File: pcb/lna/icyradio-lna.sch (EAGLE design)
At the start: 15 parts, among them U1 ADL5601

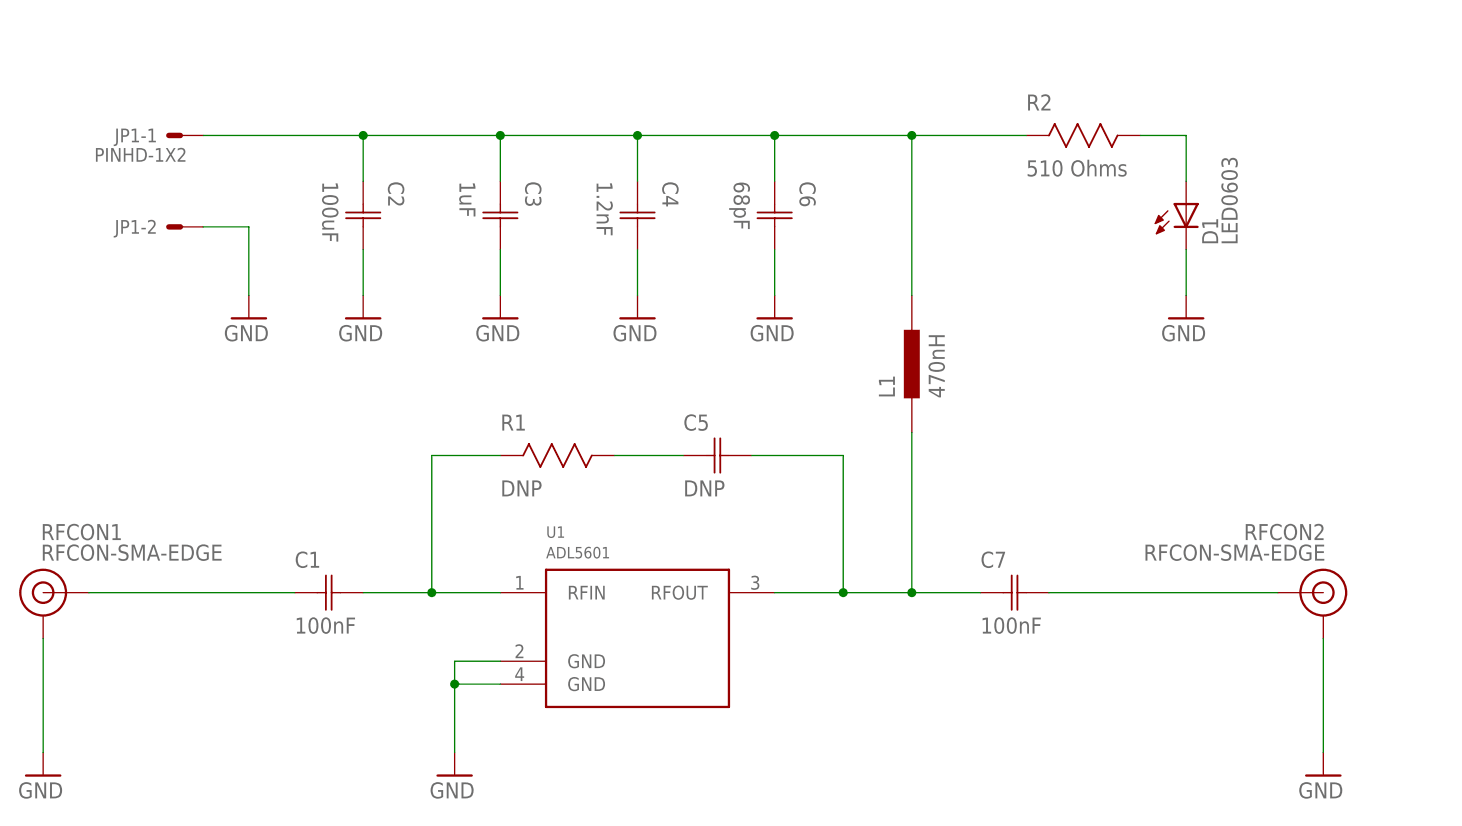
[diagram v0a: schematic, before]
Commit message: Sync library updates on LNA PCB
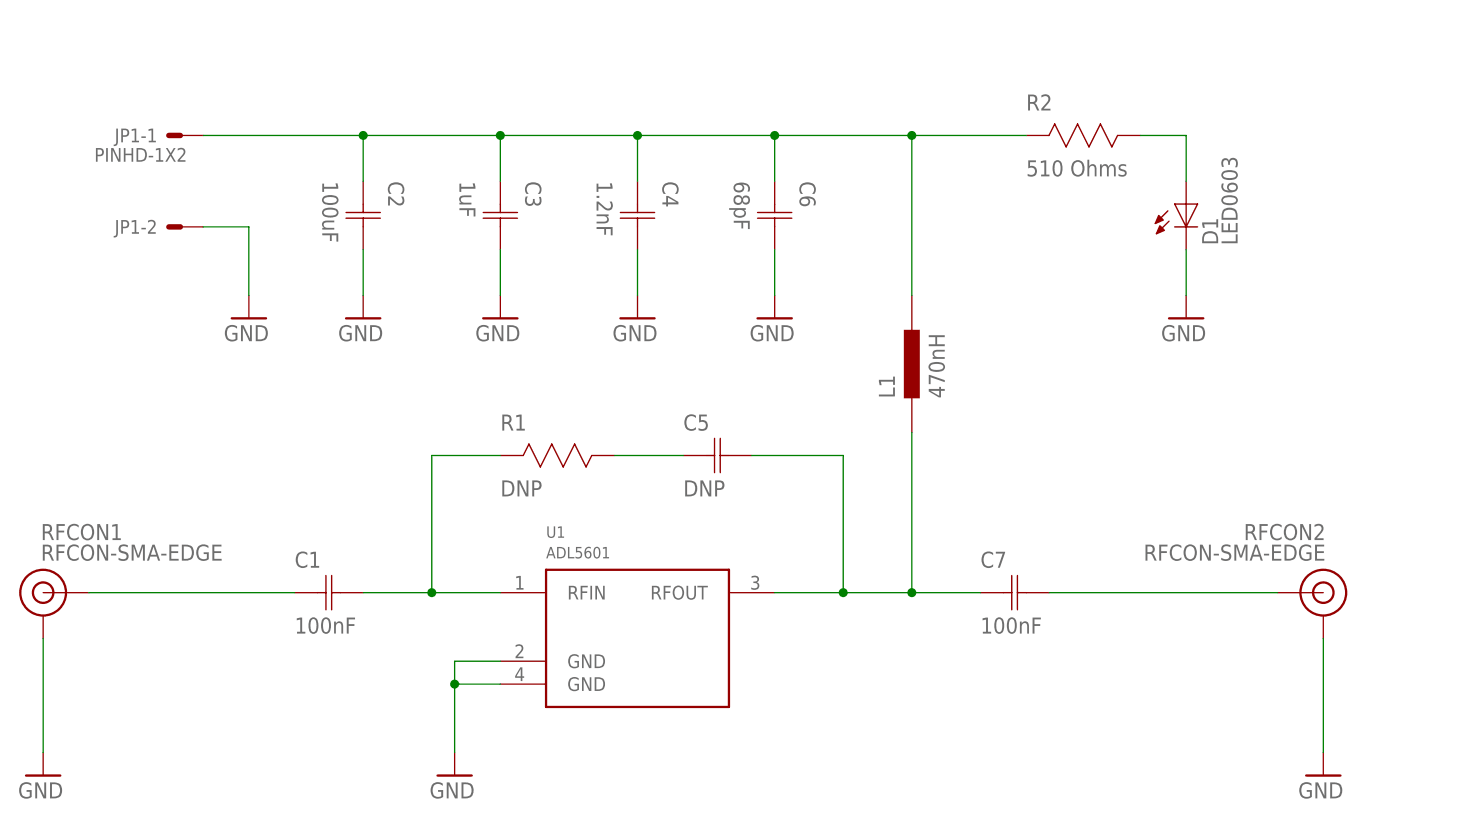
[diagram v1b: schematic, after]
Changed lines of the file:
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@@
 </classes>
 <parts>
-<part name="FRAME1" library="Frame" deviceset="A4-LANDSCAPE" device="">
-<attribute name="CNAME" value=""/>
-<attribute name="CREVISION" value=""/>
-<attribute name="DESIGNER" value=""/>
-</part>
 <part name="RFCON2" library="RF Connector" deviceset="RFCON" device="-SMA-EDGE"/>
 <part name="GND9" library="Supply Symbol" deviceset="GND" device=""/>
@@
 <part name="C2" library="Capacitor" deviceset="CAPACITOR" device="-1206" value="100uF"/>
 <part name="GND3" library="Supply Symbol" deviceset="GND" device=""/>
+<part name="FRAME1" library="Frame" deviceset="A4-LANDSCAPE" device=""/>
 </parts>
 <sheets>
@@
 </plain>
 <instances>
-<instance part="FRAME1" gate="G$1" x="0" y="0" smashed="yes">
-<attribute name="DRAWING_NAME" x="165.1" y="15.494" size="2.54" layer="94" font="vector"/>
-<attribute name="LAST_DATE_TIME" x="165.1" y="10.414" size="2.286" layer="94" font="vector"/>
-<attribute name="SHEET" x="179.07" y="5.334" size="2.54" layer="94" font="vector"/>
-<attribute name="DESIGNER" x="209.75" y="10.414" size="2.54" layer="94" font="vector"/>
-<attribute name="CNAME" x="165.1" y="20.574" size="2.54" layer="94" font="vector"/>
-<attribute name="CREVISION" x="218.41" y="5.234" size="2.54" layer="94" font="vector"/>
-</instance>
 <instance part="RFCON2" gate="G$1" x="208.28" y="86.36" smashed="yes" rot="MR0">
 <attribute name="NAME" x="208.534" y="92.202" size="1.778" layer="95" rot="MR0"/>
@@
 <attribute name="VALUE" x="98.806" y="114.3" size="1.778" layer="96"/>
 </instance>
+<instance part="FRAME1" gate="G$1" x="0" y="0" smashed="yes">
+<attribute name="DRAWING_NAME" x="165.1" y="15.494" size="2.54" layer="94" font="vector"/>
+<attribute name="LAST_DATE_TIME" x="165.1" y="10.414" size="2.286" layer="94" font="vector"/>
+<attribute name="SHEET" x="179.07" y="5.334" size="2.54" layer="94" font="vector"/>
+<attribute name="CNAME" x="165.1" y="20.574" size="2.54" layer="94" font="vector"/>
+<attribute name="DESIGNER" x="209.75" y="10.414" size="2.54" layer="94" font="vector"/>
+<attribute name="CREVISION" x="218.41" y="5.234" size="2.54" layer="94" font="vector"/>
+</instance>
 </instances>

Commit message: Tidy up HDL Add SSB modulation MATLAB script
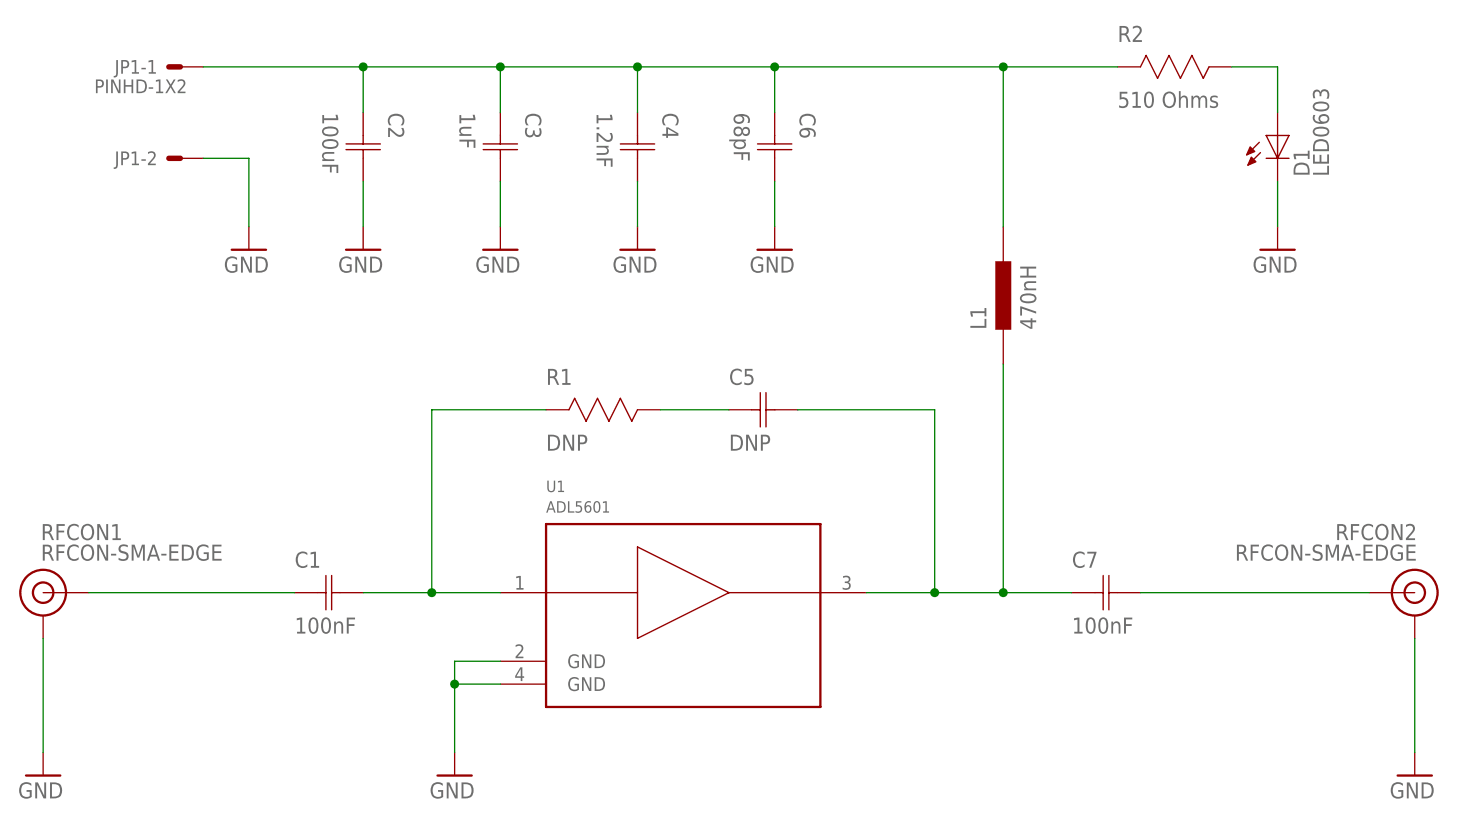
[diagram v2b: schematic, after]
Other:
- moved on the sheet: C2, C3, C4, C5, C6, C7, D1, JP1-1, JP1-2, L1, R1, R2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
